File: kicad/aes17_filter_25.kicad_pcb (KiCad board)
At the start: 4 copper layers, 175 x 90 mm, 36 parts, among them J1 NC3FAAH, J2 NC3MAAH, J3 Conn_01x01_Pin, J4 Conn_01x01_Pin, J5 Conn_01x01_Pin, SW1 SW_DPDT_x2

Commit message: closing in on final design for v2
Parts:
- added R13: 1k8, Resistor_THT:R_Axial_DIN0309_L9.0mm_D3.2mm_P12.70mm_Horizontal, F.Cu at (153.0, 101.0)
- added R14: 1k8, Resistor_THT:R_Axial_DIN0309_L9.0mm_D3.2mm_P12.70mm_Horizontal, F.Cu at (153.0, 97.2)
- C1, C2, C3, C4, C5, C6: footprint Capacitor_THT:C_Rect_L7.2mm_W5.5mm_P5.00mm_FKS2_FKP2_MKS2_MKP2 -> Capacitor_THT:C_Rect_L7.2mm_W4.5mm_P5.00mm_FKS2_FKP2_MKS2_MKP2
- C10, C7, C8, C9: footprint Capacitor_THT:C_Rect_L18.0mm_W9.0mm_P15.00mm_FKS3_FKP3 -> Capacitor_THT:C_Rect_L7.2mm_W7.2mm_P5.00mm_FKS2_FKP2_MKS2_MKP2
- R1, R2: footprint Resistor_THT:R_Axial_DIN0516_L15.5mm_D5.0mm_P20.32mm_Horizontal -> Resistor_THT:R_Axial_Power_L25.0mm_W6.4mm_P30.48mm
- R10, R9: footprint Resistor_THT:R_Axial_DIN0414_L11.9mm_D4.5mm_P20.32mm_Horizontal -> Resistor_THT:R_Axial_DIN0207_L6.3mm_D2.5mm_P10.16mm_Horizontal
- R11, R12: value 4k5 -> 2k7; footprint Resistor_THT:R_Axial_DIN0411_L9.9mm_D3.6mm_P15.24mm_Horizontal -> Resistor_THT:R_Axial_DIN0309_L9.0mm_D3.2mm_P12.70mm_Horizontal
- R3, R4: footprint Resistor_THT:R_Axial_DIN0414_L11.9mm_D4.5mm_P20.32mm_Horizontal -> Resistor_THT:R_Axial_DIN0204_L3.6mm_D1.6mm_P7.62mm_Horizontal
- R5, R6: footprint Resistor_THT:R_Axial_DIN0414_L11.9mm_D4.5mm_P20.32mm_Horizontal -> Resistor_THT:R_Axial_DIN0614_L14.3mm_D5.7mm_P20.32mm_Horizontal
- R7, R8: footprint Resistor_THT:R_Axial_DIN0411_L9.9mm_D3.6mm_P15.24mm_Horizontal -> Resistor_THT:R_Axial_DIN0204_L3.6mm_D1.6mm_P7.62mm_Horizontal
- moved R11 48.6 mm to (137.2, 101.1), turned to 180 degrees
- moved R12 48.5 mm to (137.2, 97.2), turned to 180 degrees
- moved R6 26.5 mm to (100.3, 74.9)
- moved R5 26.0 mm to (100.3, 81.3)
- moved R7 23.3 mm to (207.0, 113.0)
- moved R8 23.3 mm to (207.0, 64.8)
- moved C10 16.7 mm to (214.7, 76.1), turned to 90 degrees
- moved R2 11.5 mm to (113.2, 92.3)
- moved C8 11.0 mm to (61.6, 81.9), turned to 0 degrees
- moved C7 9.69 mm to (66.7, 96.5), turned to 180 degrees
- moved C6 8.26 mm to (76.4, 81.9)
- moved SW1 7.99 mm to (91.4, 111.2), turned to 0 degrees
- moved R9 7.73 mm to (189.2, 104.1)
- moved C4 7.62 mm to (76.4, 96.5)
- moved R10 7.62 mm to (193.0, 104.1)
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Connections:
- R11 pad 1: Net-(SW1B-C) -> Net-(R11-Pad1)
- R12 pad 1: Net-(SW1A-C) -> Net-(R12-Pad1)
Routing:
- net Net-(SW1A-C): track 12.5 -> 74.2 mm
- net Net-(SW1B-C): track 11.8 -> 65.4 mm
- net Net-(L4-Pad1): track 136.0 -> 104.6 mm
- net Net-(C3-Pad2): track 48.5 -> 67.2 mm
- net Net-(C1-Pad1): track 54.8 -> 36.8 mm
- net Net-(C9-Pad1): track 60.7 -> 45.2 mm
- net Net-(C5-Pad2): track 48.5 -> 61.9 mm
- net Net-(L3-Pad1): track 136.1 -> 124.5 mm
- net Net-(SW1A-A): track 36.3 -> 45.6 mm
- net Net-(C3-Pad1): track 21.0 -> 12.1 mm
- net Net-(C5-Pad1): track 20.9 -> 12.1 mm
- net Net-(SW1B-A): track 26.0 -> 34.7 mm
- net Net-(J3-Pin_1): track 76.6 -> 68.3 mm
- net Net-(C2-Pad2): track 54.8 -> 47.2 mm
- net Net-(J2-Pad3): track 5.61 -> 0.00 mm
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
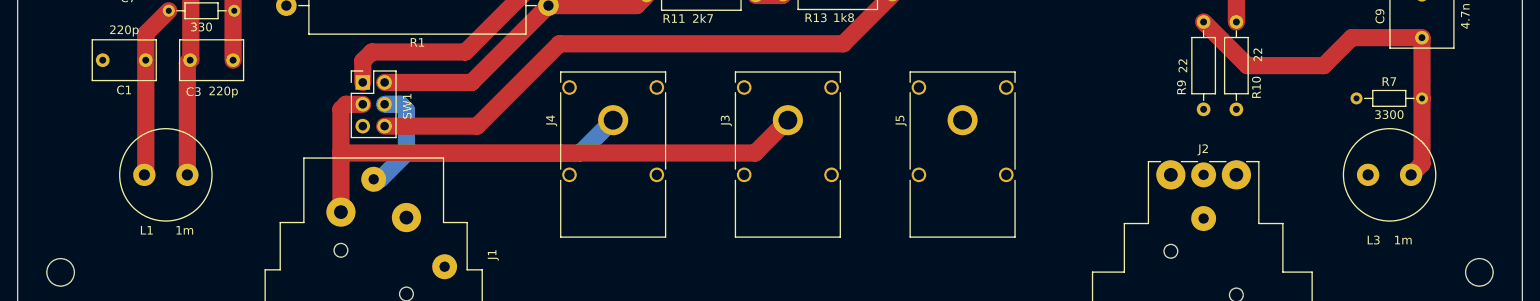
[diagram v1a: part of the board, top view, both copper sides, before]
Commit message: moved L1 and L3 further away from XLR sockets
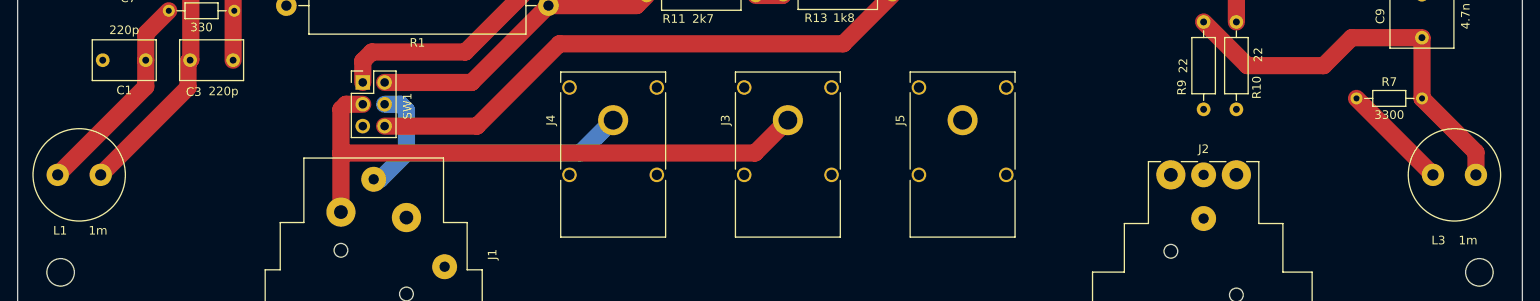
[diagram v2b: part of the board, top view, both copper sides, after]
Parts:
- moved L1 10.1 mm to (56.0, 121.9)
- moved L3 7.54 mm to (215.9, 121.9)
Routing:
- net Net-(C3-Pad2): track 67.2 -> 71.8 mm
- net Net-(C1-Pad1): track 36.8 -> 41.0 mm
- net Net-(L3-Pad1): track 124.5 -> 127.6 mm
- net Net-(C9-Pad1): track 45.2 -> 47.3 mm
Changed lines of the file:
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@@
 		(tags "Through hole pin header THT 2x03 2.54mm double row")
 		(property "Reference" "SW1"
-			(at 1.27 -2.33 360)
+			(at 1.27 -2.33 0)
 			(layer "F.SilkS")
 			(hide yes)
@@
 		(tags "C Rect series Radial pin pitch 5.00mm  length 7.2mm width 7.2mm Capacitor")
 		(property "Reference" "C10"
-			(at 2.5 -4.85 270)
+			(at 2.5 -4.85 -90)
 			(layer "F.SilkS")
 			(effects
@@
 		)
 		(property "Value" "4.7n"
-			(at 2.5 4.85 270)
+			(at 2.5 4.85 -90)
 			(layer "F.SilkS")
 			(effects
@@
 		)
 		(fp_text user "${REFERENCE}"
-			(at 2.5 0 270)
+			(at 2.5 0 -90)
 			(layer "F.Fab")
 			(effects
@@
 		)
 		(property "Value" "22"
-			(at 3.81 -2.54 270)
+			(at 3.81 -2.54 -90)
 			(layer "F.SilkS")
 			(effects
@@
 		(tags "Resistor Axial_DIN0204 series Axial Horizontal pin pitch 7.62mm 0.167W length 3.6mm diameter 1.6mm")
 		(property "Reference" "R8"
-			(at 3.81 -1.92 360)
+			(at 3.81 -1.92 0)
 			(layer "F.SilkS")
 			(effects
@@
 		)
 		(fp_text user "${REFERENCE}"
-			(at 3.81 0 360)
+			(at 3.81 0 0)
 			(layer "F.Fab")
 			(effects
@@
 		(tags "Resistor Axial_DIN0204 series Axial Horizontal pin pitch 7.62mm 0.167W length 3.6mm diameter 1.6mm")
 		(property "Reference" "R7"
-			(at 3.81 -1.92 360)
+			(at 3.81 -1.92 0)
 			(layer "F.SilkS")
 			(effects
@@
 		)
 		(property "Value" "3300"
-			(at 3.81 1.92 360)
+			(at 3.81 1.92 0)
 			(layer "F.SilkS")
 			(effects
@@
 		)
 		(fp_text user "${REFERENCE}"
-			(at 3.81 0 360)
+			(at 3.81 0 0)
 			(layer "F.Fab")
 			(effects
@@
 	(footprint "Inductor_THT:L_Radial_D10.5mm_P5.00mm_Abacron_AISR-01"
 		(layer "F.Cu")
-		(at 66.04 121.92)
+		(at 55.96 121.92)
 		(descr "Inductor, Radial series, Radial, pin pitch=5.00mm, , diameter=10.5mm, Abacron, AISR-01, http://www.abracon.com/Magnetics/radial/AISR-01.pdf")
 		(tags "Inductor Radial series Radial pin pitch 5.00mm  diameter 10.5mm Abacron AISR-01")
@@
 		)
 		(property "Value" "22"
-			(at 5.08 2.37 270)
+			(at 5.08 2.37 -90)
 			(layer "F.SilkS")
 			(effects
@@
 		(tags "C Rect series Radial pin pitch 5.00mm  length 7.2mm width 7.2mm Capacitor")
 		(property "Reference" "C9"
-			(at 2.5 -4.85 270)
+			(at 2.5 -4.85 -90)
 			(layer "F.SilkS")
 			(effects
@@
 		)
 		(property "Value" "4.7n"
-			(at 2.5 5.08 270)
+			(at 2.5 5.08 -90)
 			(layer "F.SilkS")
 			(effects
@@
 		)
 		(fp_text user "${REFERENCE}"
-			(at 2.5 0 270)
+			(at 2.5 0 -90)
 			(layer "F.Fab")
 			(effects
@@
 	(footprint "Inductor_THT:L_Radial_D10.5mm_P5.00mm_Abacron_AISR-01"
 		(layer "F.Cu")
-		(at 208.36 121.92)
+		(at 215.9 121.92)
 		(descr "Inductor, Radial series, Radial, pin pitch=5.00mm, , diameter=10.5mm, Abacron, AISR-01, http://www.abracon.com/Magnetics/radial/AISR-01.pdf")
 		(tags "Inductor Radial series Radial pin pitch 5.00mm  diameter 10.5mm Abacron AISR-01")
 		(property "Reference" "L3"
-			(at 0.635 7.62 360)
+			(at 0.635 7.62 0)
 			(layer "F.SilkS")
 			(effects
@@
 		)
 		(property "Value" "1m"
-			(at 4.081051 7.62 360)
+			(at 4.081051 7.62 0)
 			(layer "F.SilkS")
 			(effects
@@
 		)
 		(fp_text user "${REFERENCE}"
-			(at 2.5 -2.54 360)
+			(at 2.5 -2.54 0)
 			(layer "F.Fab")
 			(effects
@@
 		(tags "C Rect series Radial pin pitch 5.00mm  length 7.2mm width 7.2mm Capacitor")
 		(property "Reference" "C8"
-			(at 2.5 -4.85 360)
+			(at 2.5 -4.85 0)
 			(layer "F.SilkS")
 			(effects
@@
 		)
 		(fp_text user "${REFERENCE}"
-			(at 2.5 0 360)
+			(at 2.5 0 0)
 			(layer "F.Fab")
 			(effects
@@
 	)
 	(segment
+		(start 71.36 108.585)
+		(end 71.12 108.825)
+		(width 2)
+		(layer "F.Cu")
+		(net 4)
+	)
+	(segment
 		(start 71.44 96.52)
 		(end 71.44 108.505)
@@
 	)
 	(segment
-		(start 71.04 108.905)
-		(end 71.04 121.92)
+		(start 71.12 108.825)
+		(end 71.12 111.76)
 		(width 2)
 		(layer "F.Cu")
@@
 	)
 	(segment
+		(start 71.12 111.76)
+		(end 60.96 121.92)
+		(width 2)
+		(layer "F.Cu")
+		(net 4)
+	)
+	(segment
 		(start 71.44 96.52)
 		(end 71.44 93.66)
@@
 	)
 	(segment
-		(start 214.63 120.65)
-		(end 214.63 113.03)
+		(start 203.2 109.22)
+		(end 194.31 109.22)
 		(width 2)
 		(layer "F.Cu")
@@
 	)
 	(segment
-		(start 213.36 121.92)
-		(end 214.63 120.65)
+		(start 214.62015 105.968556)
+		(end 206.451444 105.968556)
 		(width 2)
 		(layer "F.Cu")
@@
 	)
 	(segment
-		(start 203.2 109.22)
-		(end 194.31 109.22)
+		(start 214.63 113.03)
+		(end 220.9 119.3)
 		(width 2)
 		(layer "F.Cu")
@@
 	)
 	(segment
-		(start 214.62015 105.968556)
-		(end 206.451444 105.968556)
+		(start 206.451444 105.968556)
+		(end 203.2 109.22)
 		(width 2)
 		(layer "F.Cu")
@@
 	)
 	(segment
-		(start 206.451444 105.968556)
-		(end 203.2 109.22)
+		(start 194.31 109.22)
+		(end 189.23 104.14)
 		(width 2)
 		(layer "F.Cu")
@@
 	)
 	(segment
-		(start 194.31 109.22)
-		(end 189.23 104.14)
+		(start 220.9 119.3)
+		(end 220.9 121.92)
 		(width 2)
 		(layer "F.Cu")
@@
 	)
 	(segment
-		(start 208.36 114.38)
-		(end 207.01 113.03)
+		(start 207.01 113.03)
+		(end 215.9 121.92)
 		(width 2)
-		(layer "In2.Cu")
+		(layer "F.Cu")
 		(net 13)
 	)
@@
 	)
 	(segment
-		(start 208.36 121.92)
-		(end 208.36 114.38)
-		(width 2)
-		(layer "In2.Cu")
-		(net 13)
-	)
-	(segment
 		(start 207.01 90.17)
 		(end 207.01 113.03)
@@
 	(segment
 		(start 66.2 108.585)
-		(end 66.2 121.76)
+		(end 66.2 105.51785)
 		(width 2)
 		(layer "F.Cu")
@@
 	)
 	(segment
-		(start 66.2 108.585)
-		(end 66.2 105.51785)
+		(start 66.2 111.68)
+		(end 55.96 121.92)
 		(width 2)
 		(layer "F.Cu")
@@
 	)
 	(segment
-		(start 66.2 121.76)
-		(end 66.04 121.92)
+		(start 66.2 105.51785)
+		(end 68.879012 102.838838)
 		(width 2)
 		(layer "F.Cu")
@@
 	)
 	(segment
-		(start 66.2 105.51785)
-		(end 68.879012 102.838838)
+		(start 66.2 108.585)
+		(end 66.2 111.68)
 		(width 2)
 		(layer "F.Cu")

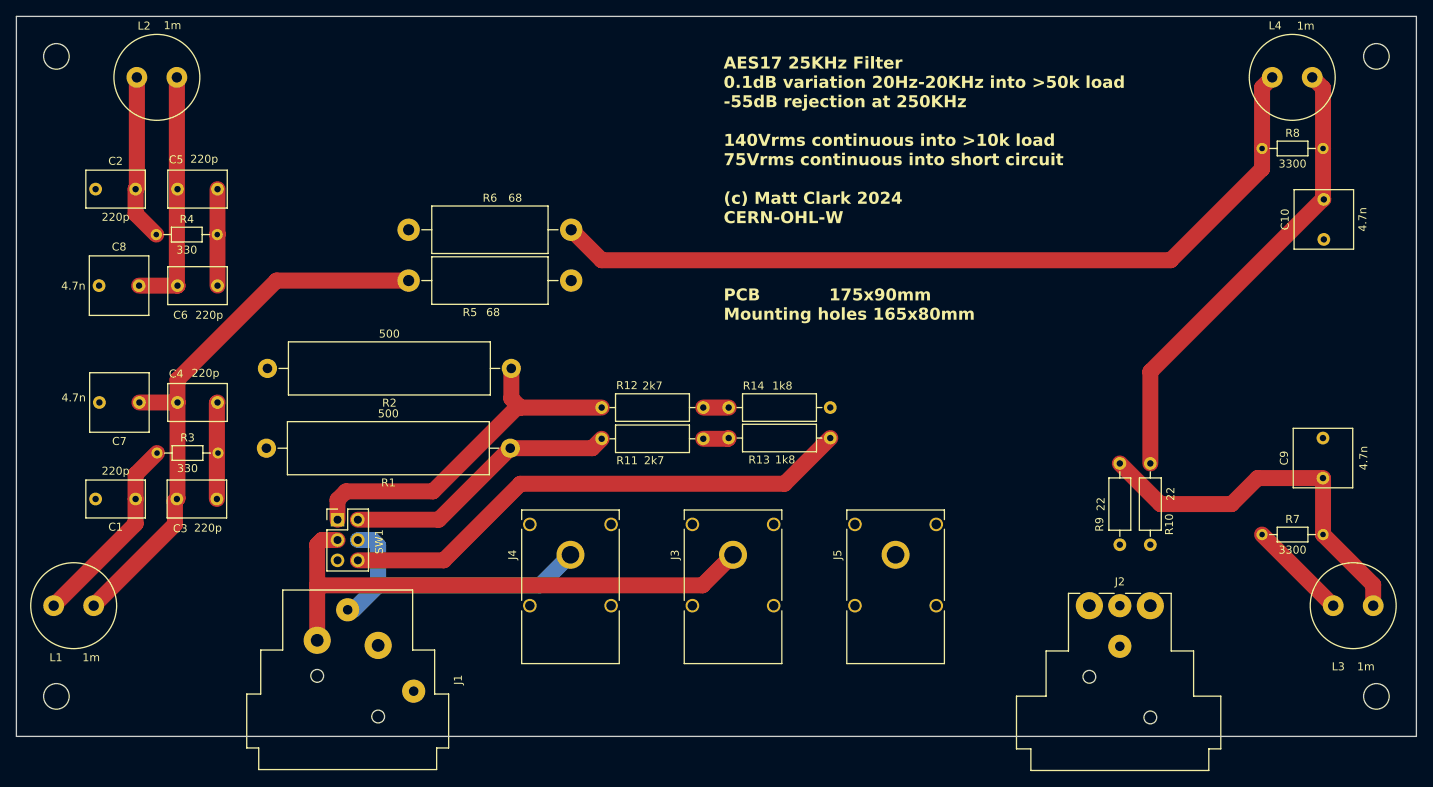
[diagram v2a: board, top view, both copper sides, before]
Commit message: added post-filter attenuator network
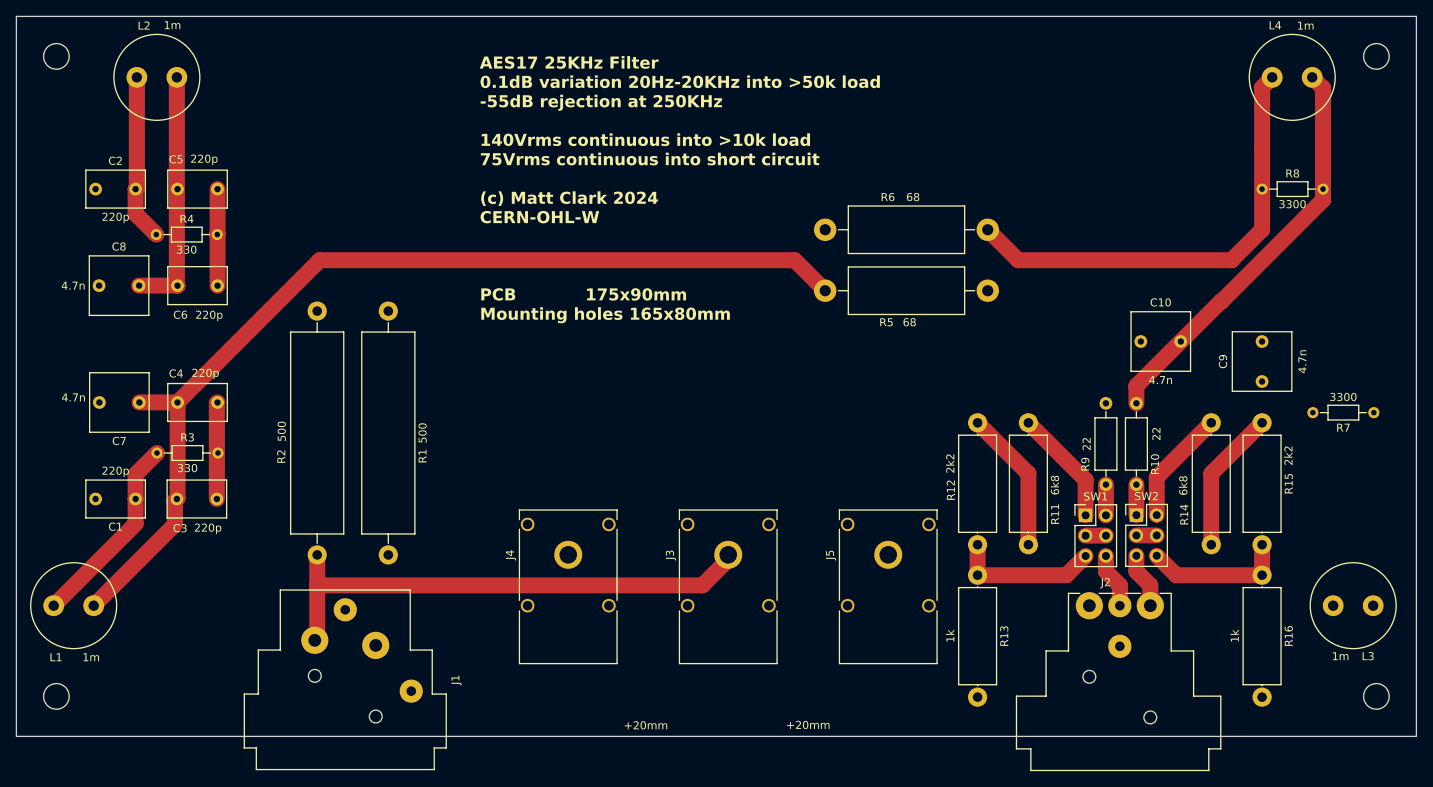
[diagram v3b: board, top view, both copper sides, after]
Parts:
- added R15: 2k2, Resistor_THT:R_Axial_DIN0414_L11.9mm_D4.5mm_P15.24mm_Horizontal, F.Cu at (207.0, 99.1)
- added R16: 1k, Resistor_THT:R_Axial_DIN0414_L11.9mm_D4.5mm_P15.24mm_Horizontal, F.Cu at (207.0, 118.1)
- added SW2: SW_DPDT_x2, Connector_PinHeader_2.54mm:PinHeader_2x03_P2.54mm_Vertical, F.Cu at (191.3, 110.6)
- R11: value 2k7 -> 6k8; footprint Resistor_THT:R_Axial_DIN0309_L9.0mm_D3.2mm_P12.70mm_Horizontal -> Resistor_THT:R_Axial_DIN0414_L11.9mm_D4.5mm_P15.24mm_Horizontal
- R12: value 2k7 -> 2k2; footprint Resistor_THT:R_Axial_DIN0309_L9.0mm_D3.2mm_P12.70mm_Horizontal -> Resistor_THT:R_Axial_DIN0414_L11.9mm_D4.5mm_P15.24mm_Horizontal
- R13: value 1k8 -> 1k; footprint Resistor_THT:R_Axial_DIN0309_L9.0mm_D3.2mm_P12.70mm_Horizontal -> Resistor_THT:R_Axial_DIN0414_L11.9mm_D4.5mm_P15.24mm_Horizontal
- R14: value 1k8 -> 6k8; footprint Resistor_THT:R_Axial_DIN0309_L9.0mm_D3.2mm_P12.70mm_Horizontal -> Resistor_THT:R_Axial_DIN0414_L11.9mm_D4.5mm_P15.24mm_Horizontal
- moved SW1 93.5 mm to (185.0, 110.6)
- moved R5 52.1 mm to (152.4, 82.5)
- moved R6 52.1 mm to (152.4, 74.9)
- moved R14 47.7 mm to (200.7, 99.1), turned to -90 degrees
- moved R11 40.7 mm to (177.8, 99.1), turned to -90 degrees
- moved R12 34.3 mm to (171.4, 99.1), turned to -90 degrees
- moved R2 33.6 mm to (88.9, 115.6), turned to 90 degrees
- moved C10 26.2 mm to (191.8, 88.9), turned to 0 degrees
- moved R13 25.2 mm to (171.4, 118.1), turned to -90 degrees
- moved R7 20.7 mm to (221.0, 97.8), turned to 180 degrees
- moved R1 20.3 mm to (97.8, 115.6), turned to 90 degrees
- moved C9 14.3 mm to (207.0, 93.9)
- moved R10 7.71 mm to (191.3, 96.6)
- moved R9 7.71 mm to (187.5, 96.6)
- moved R8 5.08 mm to (207.0, 69.8)
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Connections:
- J2 pad 2: Net-(J2-Pad2) -> Net-(SW2B-B)
- J2 pad 3: Net-(J2-Pad3) -> Net-(SW1B-B)
- R1 pad 1: Net-(SW1B-A) -> Net-(J4-Pin_1)
- R10 pad 2: Net-(J2-Pad2) -> Net-(SW2A-B)
- R11 pad 1: Net-(R11-Pad1) -> Net-(SW1A-A)
- R11 pad 2: Net-(SW1B-A) -> Net-(R11-Pad2)
- R12 pad 1: Net-(R12-Pad1) -> Net-(R11-Pad2)
- R12 pad 2: Net-(SW1A-A) -> Net-(SW1B-C)
- R13 pad 2: Net-(R11-Pad1) -> GND
- R14 pad 1: Net-(SW1A-C) -> Net-(SW2A-A)
- R14 pad 2: Net-(R12-Pad1) -> Net-(R14-Pad2)
- R2 pad 1: Net-(SW1A-A) -> Net-(J3-Pin_1)
- R9 pad 2: Net-(J2-Pad3) -> Net-(SW1A-B)
- SW1 pad 2: Net-(J3-Pin_1) -> Net-(SW1A-B)
- SW1 pad 4: Net-(SW1B-A) -> Net-(SW1A-C)
- SW1 pad 5: Net-(J4-Pin_1) -> Net-(SW1B-C)
- SW1 pad 6: Net-(SW1B-C) -> Net-(SW1B-B)
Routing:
- net Net-(SW1A-C): track 74.2 -> 2.54 mm
- net Net-(C5-Pad2): track 61.9 -> 117.1 mm
- net Net-(C3-Pad2): track 71.8 -> 124.9 mm
- net Net-(L4-Pad1): track 104.6 -> 57.0 mm
- net Net-(SW1B-C): track 65.4 -> 18.3 mm
- net Net-(L3-Pad1): track 127.6 -> 82.6 mm
- net Net-(SW1B-A): track 34.7 -> 0.00 mm
- net Net-(SW1A-A): track 45.6 -> 14.5 mm
- net Net-(C1-Pad1): track 41.0 -> 60.7 mm
- net Net-(SW2B-C): track 0.00 -> 18.0 mm
- net Net-(R11-Pad2): track 0.00 -> 17.9 mm
- net Net-(R14-Pad2): track 0.00 -> 17.9 mm
- net Net-(SW2A-A): track 0.00 -> 14.4 mm
- net Net-(SW2B-B): track 0.00 -> 6.96 mm
- net Net-(SW1B-B): track 0.00 -> 6.93 mm
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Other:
- board text added: "+20mm"
